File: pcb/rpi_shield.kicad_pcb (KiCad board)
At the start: 2 copper layers, 65 x 56 mm, 61 parts, among them P101 CONN_01X08, P102 CONN_02X20, P301 USB_OTG, Q201 Q_NMOS_GDSD, Q202 Q_NMOS_GDSD, Q203 Q_NMOS_GDSD, Q204 Q_NMOS_GDSD, Q205 NPN, Q206 NPN, Q207 NPN, Q208 NPN, Q301 FT230XS-R, U201 LM2902N, U202 MAX5813

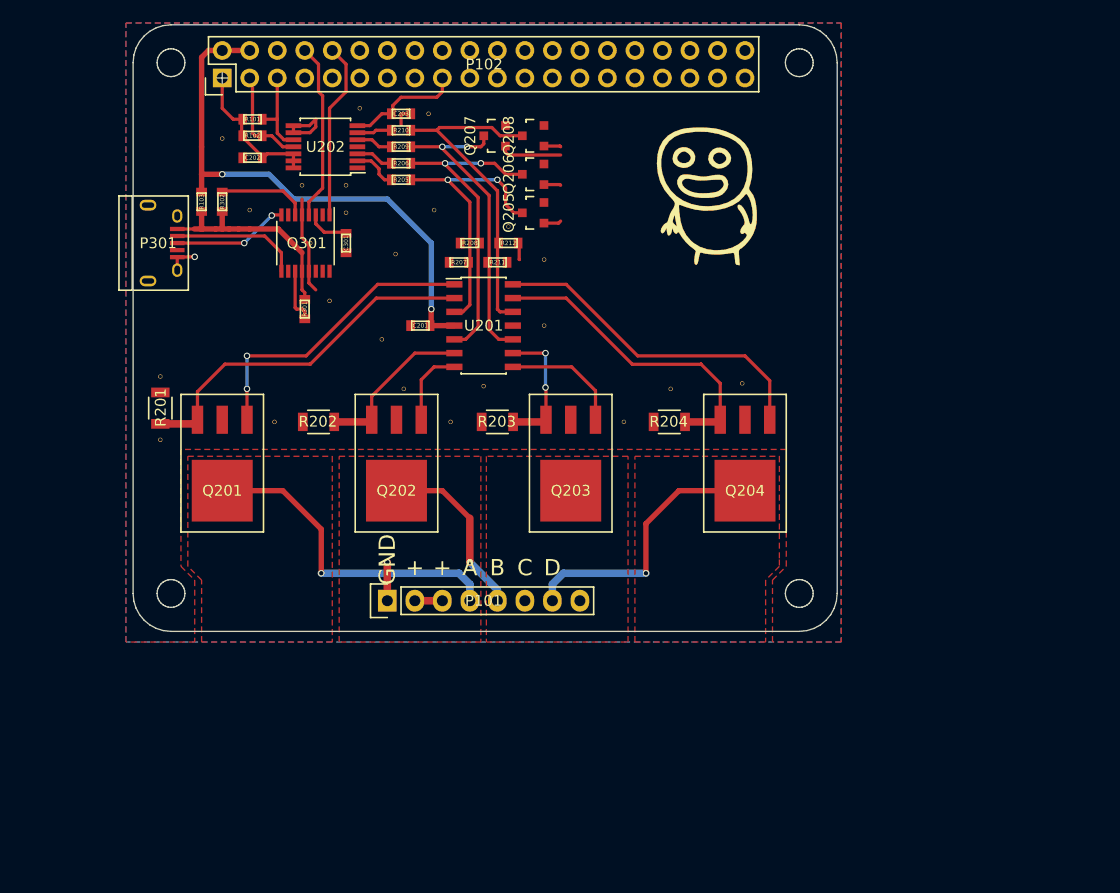
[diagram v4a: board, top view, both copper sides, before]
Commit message: removed resistor dividors, added cap to usb
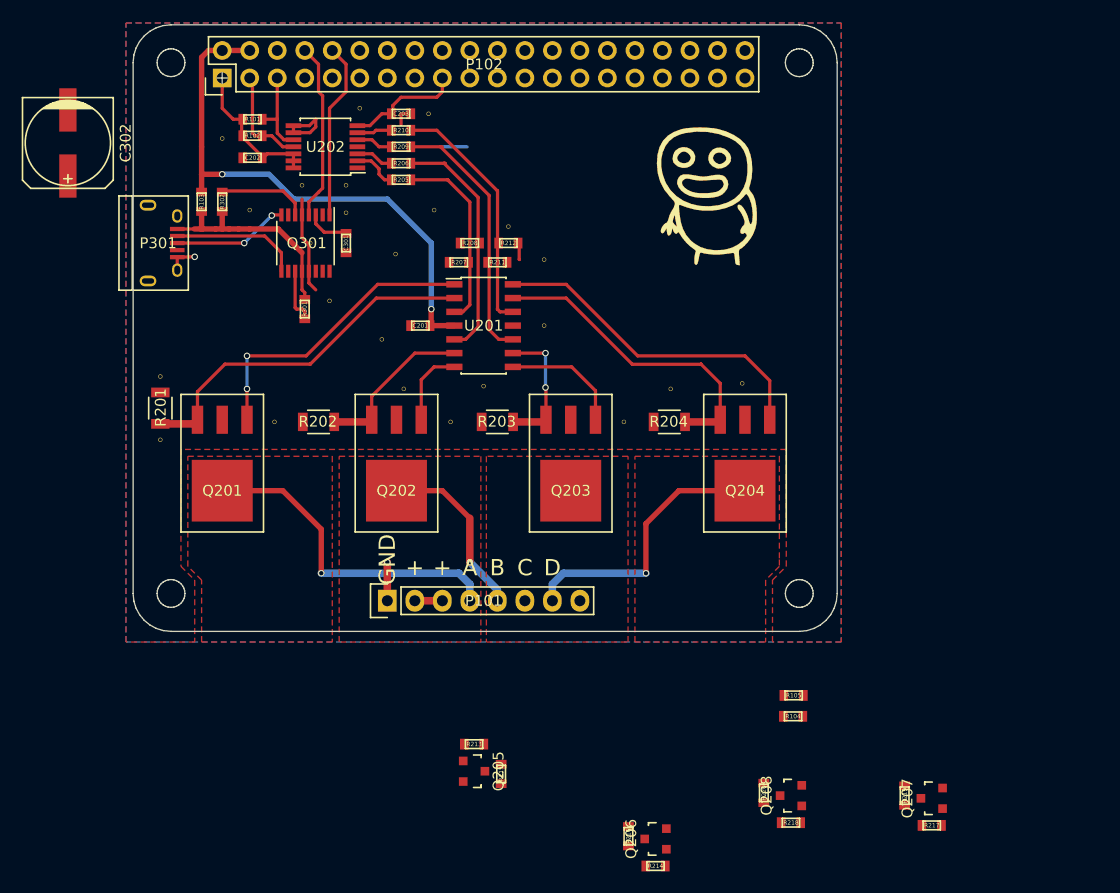
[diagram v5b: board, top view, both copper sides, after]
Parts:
- added C302: CP, Capacitors_SMD:c_elec_8x5.4, F.Cu at (115.8, 86.0)
- added R104: R, netl:SMD_0603, F.Cu at (182.7, 138.9)
- added R105: R, netl:SMD_0603, F.Cu at (182.8, 137.0)
- added R213: R, netl:SMD_0603, F.Cu at (153.2, 141.5)
- added R214: R, netl:SMD_0603, F.Cu at (170.0, 152.8)
- added R215: R, netl:SMD_0603, F.Cu at (155.8, 144.2)
- added R216: R, netl:SMD_0603, F.Cu at (167.5, 150.0)
- added R217: R, netl:SMD_0603, F.Cu at (195.5, 149.0)
- added R218: R, netl:SMD_0603, F.Cu at (182.5, 148.8)
- added R219: R, netl:SMD_0603, F.Cu at (193.0, 146.2)
- added R220: R, netl:SMD_0603, F.Cu at (180.0, 146.0)
- moved Q207 73.3 mm to (195.5, 146.5)
- moved Q208 65.4 mm to (182.5, 146.2)
- moved Q206 62.4 mm to (170.0, 150.2)
- moved Q205 51.8 mm to (153.2, 144.0), turned to 270 degrees
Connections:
- net MISO renamed /MISO
- net MOSI renamed /MOSI
- net RESET renamed /RESET
- net SCK renamed /SCK
- P102 pad 3: /LED driver/SDA -> /SDA
- P102 pad 5: /LED driver/SCL -> /SCL
- Q205 pad 3: Net-(Q205-Pad3) -> Net-(Q201-Pad1)
- Q206 pad 3: Net-(Q206-Pad3) -> Net-(Q202-Pad1)
- Q207 pad 3: Net-(Q207-Pad3) -> Net-(Q203-Pad1)
- Q208 pad 3: Net-(Q208-Pad3) -> Net-(Q204-Pad1)
- R101 pad 2: /LED driver/SCL -> /SDA
- R102 pad 2: /LED driver/SDA -> /SCL
- R205 pad 1: Net-(Q205-Pad3) -> Net-(R205-Pad1)
- R206 pad 1: Net-(Q206-Pad3) -> Net-(R206-Pad1)
- R207 pad 1: Net-(Q205-Pad3) -> Net-(R205-Pad1)
- R208 pad 1: Net-(Q206-Pad3) -> Net-(R206-Pad1)
- R209 pad 1: Net-(Q207-Pad3) -> Net-(R209-Pad1)
- R210 pad 1: Net-(Q208-Pad3) -> Net-(R210-Pad1)
- R211 pad 1: Net-(Q207-Pad3) -> Net-(R209-Pad1)
- R212 pad 1: Net-(Q208-Pad3) -> Net-(R210-Pad1)
- U201 pad 1: Net-(Q201-Pad1) -> Net-(R215-Pad2)
- U201 pad 10: Net-(Q207-Pad3) -> /LED driver/C
- U201 pad 12: Net-(Q208-Pad3) -> /LED driver/D
- U201 pad 14: Net-(Q204-Pad1) -> Net-(R220-Pad2)
- U201 pad 3: Net-(Q205-Pad3) -> /LED driver/A
- U201 pad 5: Net-(Q206-Pad3) -> /LED driver/B
- U201 pad 7: Net-(Q202-Pad1) -> Net-(R216-Pad2)
- U201 pad 8: Net-(Q203-Pad1) -> Net-(R219-Pad2)
- U202 pad 10: /LED driver/SCL -> /SCL
- U202 pad 11: /LED driver/SDA -> /SDA
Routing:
- net Net-(Q208-Pad3): track 31.0 -> 0.00 mm
- net Net-(Q206-Pad3): track 30.4 -> 0.00 mm, vias 2 -> 0
- net Net-(Q207-Pad3): track 29.2 -> 0.00 mm, vias 2 -> 0
- net Net-(Q205-Pad3): track 26.5 -> 0.00 mm, vias 2 -> 0
- net Net-(R209-Pad1): track 0.00 -> 21.9 mm
- net Net-(R210-Pad1): track 0.00 -> 21.1 mm
- net Net-(R206-Pad1): track 0.00 -> 20.1 mm
- net Net-(R215-Pad2): track 0.00 -> 16.4 mm
- net Net-(Q201-Pad1): track 28.1 -> 11.7 mm
- net Net-(R205-Pad1): track 0.00 -> 15.8 mm
- net /SDA: track 0.00 -> 11.4 mm
- net /LED driver/SDA: track 9.49 -> 0.00 mm
- net /LED driver/SCL: track 8.12 -> 0.00 mm
- net /SCL: track 0.00 -> 6.21 mm
- net Net-(Q207-Pad1): track 5.77 -> 0.00 mm
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
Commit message: added mcu
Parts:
- removed R205, R206, R207, R208, R209, R210, R211, R212: 10k, netl:SMD_0603
- removed the VIA at (178.0, 108.2)
- removed the VIA at (124.3, 113.4)
- removed the VIA at (156.4, 93.7)
- removed the VIA at (149.6, 92.2)
- removed the VIA at (130.0, 85.6)
- removed the VIA at (154.1, 108.4)
- removed the VIA at (159.7, 96.8)
- removed the VIA at (149.1, 83.3)
- removed the VIA at (159.7, 102.9)
- removed the VIA at (146.0, 96.3)
- removed the VIA at (142.7, 82.8)
- removed the VIA at (141.4, 89.9)
- removed the VIA at (137.4, 89.9)
- removed the VIA at (141.4, 92.4)
- removed the VIA at (171.4, 108.7)
- removed the VIA at (146.8, 108.7)
- removed the VIA at (144.7, 104.1)
- removed the VIA at (139.9, 100.6)
- removed the VIA at (132.5, 92.2)
- added C401: C, netl:SMD_0603, F.Cu at (155.4, 100.0)
- added IC401: ATMEGA48-M, Housings_QFP:TQFP-32_7x7mm_Pitch0.8mm, F.Cu at (155.0, 92.5)
- added P401: CONN_01X01, netl:1Pin_small, F.Cu at (155.0, 86.0)
- added P402: CONN_01X01, netl:1Pin_small, F.Cu at (157.0, 86.0)
- added P403: CONN_01X01, netl:1Pin_small, F.Cu at (153.0, 86.0)
- added P404: CONN_01X01, netl:1Pin_small, F.Cu at (163.0, 91.0)
- added P405: CONN_01X01, netl:1Pin_small, F.Cu at (163.0, 89.0)
- added P406: CONN_01X01, netl:1Pin_small, F.Cu at (163.0, 87.0)
- added P407: CONN_01X01, netl:1Pin_small, F.Cu at (158.0, 100.0)
- added P408: CONN_01X01, netl:1Pin_small, F.Cu at (160.0, 100.0)
- added P409: CONN_01X01, netl:1Pin_small, F.Cu at (149.0, 100.0)
- added P410: CONN_01X01, netl:1Pin_small, F.Cu at (151.0, 100.0)
- added P411: CONN_01X01, netl:1Pin_small, F.Cu at (153.0, 100.0)
- added P412: CONN_01X01, netl:1Pin_small, F.Cu at (163.0, 97.0)
- added P413: CONN_01X01, netl:1Pin_small, F.Cu at (163.0, 95.0)
- added P414: CONN_01X01, netl:1Pin_small, F.Cu at (163.0, 93.0)
- added VIA: via, netl:via, F.Cu at (124.7, 122.8)
- added VIA: via, netl:via, F.Cu at (157.7, 102.4)
- added VIA: via, netl:via, F.Cu at (149.9, 102.4)
- added VIA: via, netl:via, F.Cu at (140.9, 103.2)
- added VIA: via, netl:via, F.Cu at (144.9, 108.2)
- added VIA: via, netl:via, F.Cu at (128.9, 108.2)
- added VIA: via, netl:via, F.Cu at (177.1, 108.6)
- added VIA: via, netl:via, F.Cu at (181.1, 105.4)
- added VIA: via, netl:via, F.Cu at (160.9, 107.6)
- added VIA: via, netl:via, F.Cu at (174.9, 102.0)
- added VIA: via, netl:via, F.Cu at (176.8, 89.6)
- added VIA: via, netl:via, F.Cu at (137.5, 115.8)
- added VIA: via, netl:via, F.Cu at (174.2, 90.4)
- added VIA: via, netl:via, F.Cu at (171.9, 94.6)
- added VIA: via, netl:via, F.Cu at (177.8, 94.6)
- added VIA: via, netl:via, F.Cu at (182.5, 102.2)
- added VIA: via, netl:via, F.Cu at (167.1, 101.2)
- added VIA: via, netl:via, F.Cu at (179.3, 102.0)
- added VIA: via, netl:via, F.Cu at (173.3, 108.8)
- added VIA: via, netl:via, F.Cu at (140.9, 108.2)
- added VIA: via, netl:via, F.Cu at (132.9, 101.6)
- added VIA: via, netl:via, F.Cu at (146.3, 97.0)
- added VIA: via, netl:via, F.Cu at (152.7, 116.0)
- added VIA: via, netl:via, F.Cu at (150.5, 97.0)
- added VIA: via, netl:via, F.Cu at (159.3, 97.0)
- added VIA: via, netl:via, F.Cu at (154.5, 92.4)
- added VIA: via, netl:via, F.Cu at (151.7, 85.0)
- added VIA: via, netl:via, F.Cu at (164.3, 85.2)
- added VIA: via, netl:via, F.Cu at (171.9, 85.2)
- added VIA: via, netl:via, F.Cu at (171.9, 82.2)
- added VIA: via, netl:via, F.Cu at (164.3, 82.2)
- added VIA: via, netl:via, F.Cu at (151.7, 82.2)
- added VIA: via, netl:via, F.Cu at (143.5, 82.2)
- added VIA: via, netl:via, F.Cu at (169.5, 115.8)
- added VIA: via, netl:via, F.Cu at (137.7, 82.2)
- added VIA: via, netl:via, F.Cu at (139.5, 85.6)
- added VIA: via, netl:via, F.Cu at (129.7, 83.6)
- added VIA: via, netl:via, F.Cu at (136.9, 89.2)
- added VIA: via, netl:via, F.Cu at (143.7, 91.6)
- added VIA: via, netl:via, F.Cu at (142.9, 94.2)
- added VIA: via, netl:via, F.Cu at (134.1, 97.2)
- added VIA: via, netl:via, F.Cu at (128.7, 97.8)
- added VIA: via, netl:via, F.Cu at (131.3, 95.8)
- added VIA: via, netl:via, F.Cu at (133.9, 93.4)
- added VIA: via, netl:via, F.Cu at (183.5, 121.6)
- added VIA: via, netl:via, F.Cu at (177.1, 84.8)
- added VIA: via, netl:via, F.Cu at (167.5, 94.6)
- added VIA: via, netl:via, F.Cu at (162.7, 99.4)
- added VIA: via, netl:via, F.Cu at (157.7, 107.6)
- moved R104 57.1 mm to (146.2, 95.0)
- moved R105 57.0 mm to (146.2, 93.2)
- moved R217 53.2 mm to (163.2, 106.8), turned to 0 degrees
- moved R214 51.3 mm to (147.2, 106.8), turned to 0 degrees
- moved Q207 49.3 mm to (163.2, 109.2), turned to 270 degrees
- moved Q206 46.9 mm to (147.2, 109.2), turned to 270 degrees
- moved R219 46.8 mm to (165.8, 108.2)
- moved R216 45.4 mm to (149.8, 108.2)
- moved R215 42.2 mm to (133.8, 108.2), turned to 90 degrees
- moved R218 41.9 mm to (179.5, 107.0), turned to 0 degrees
- moved Q205 41.1 mm to (131.2, 109.2)
- moved R213 41.1 mm to (131.2, 106.8)
- moved C202 38.6 mm to (171.4, 88.0), turned to 90 degrees
- moved R220 37.6 mm to (182.0, 108.5)
- moved Q208 36.9 mm to (179.5, 109.5), turned to 270 degrees
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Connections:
- net /SCL renamed /LED driver/SCL
- net /SDA renamed /LED driver/SDA
- P102 pad 15: /RESET -> /MicroController/~RESET
- P102 pad 19: /MOSI -> /MicroController/MOSI
- P102 pad 21: /MISO -> /MicroController/MISO
- P102 pad 23: /SCK -> /MicroController/SCK
- R104 pad 2: Net-(R104-Pad2) -> /MicroController/TX
- R105 pad 2: Net-(R105-Pad2) -> /MicroController/RX
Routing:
- net /LED driver/SCL: track 6.21 -> 60.5 mm, vias 0 -> 2
- net /LED driver/SDA: track 11.4 -> 59.7 mm
- net /LED driver/PWMD: track 0.00 -> 46.8 mm, vias 0 -> 2
- net /LED driver/PWMA: track 0.00 -> 39.8 mm, vias 0 -> 2
- net 3v3: track 24.3 -> 59.9 mm, vias 0 -> 2
- net /LED driver/PWMC: track 0.00 -> 33.1 mm, vias 0 -> 2
- net Net-(R215-Pad2): track 16.4 -> 44.0 mm, vias 0 -> 2
- net Net-(Q202-Pad3): track 15.1 -> 40.7 mm
- net Net-(Q201-Pad3): track 33.7 -> 58.4 mm
- net /LED driver/PWMB: track 0.00 -> 23.2 mm, vias 0 -> 2
- net Net-(R216-Pad2): track 1.87 -> 24.0 mm
- net Net-(R209-Pad1): track 21.9 -> 0.00 mm
- net Net-(R210-Pad1): track 21.1 -> 0.00 mm
- net Net-(Q204-Pad1): track 26.6 -> 5.95 mm
- net Net-(R206-Pad1): track 20.1 -> 0.00 mm
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
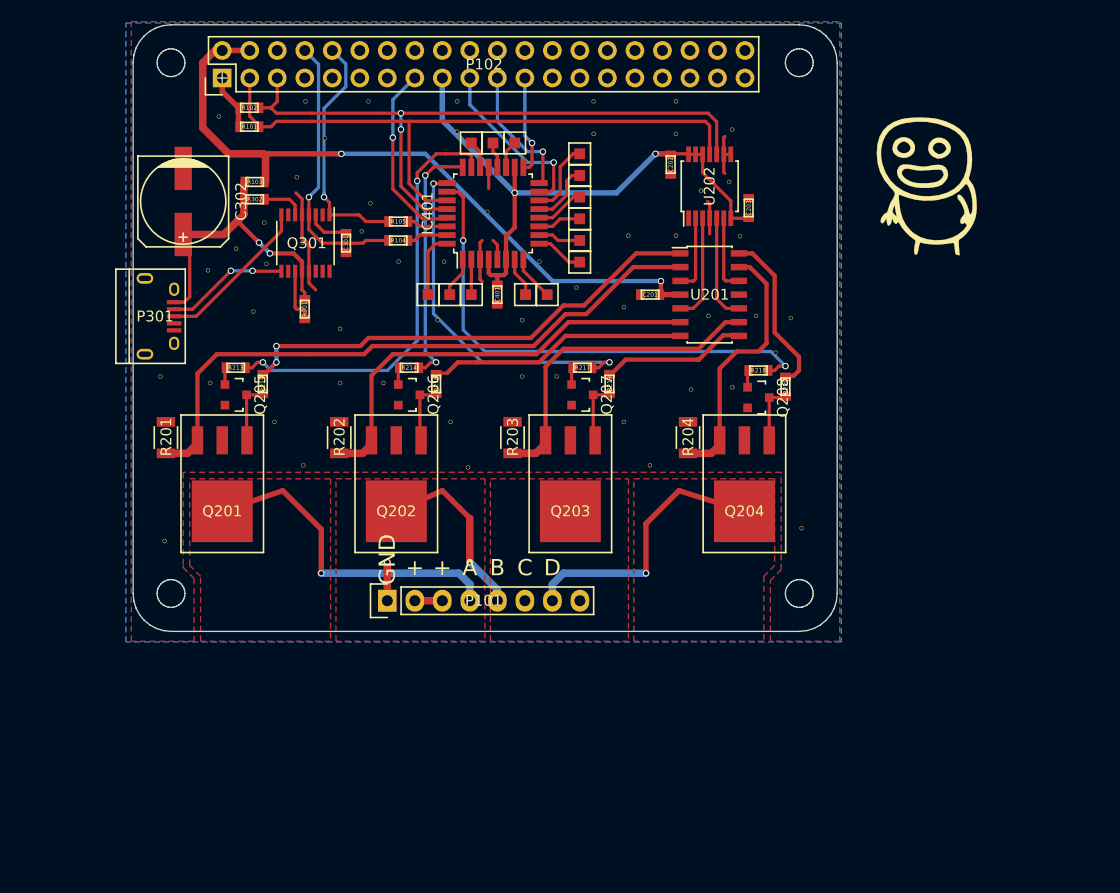
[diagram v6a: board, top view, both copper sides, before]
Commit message: added the voltage dividers back to the constant-current control
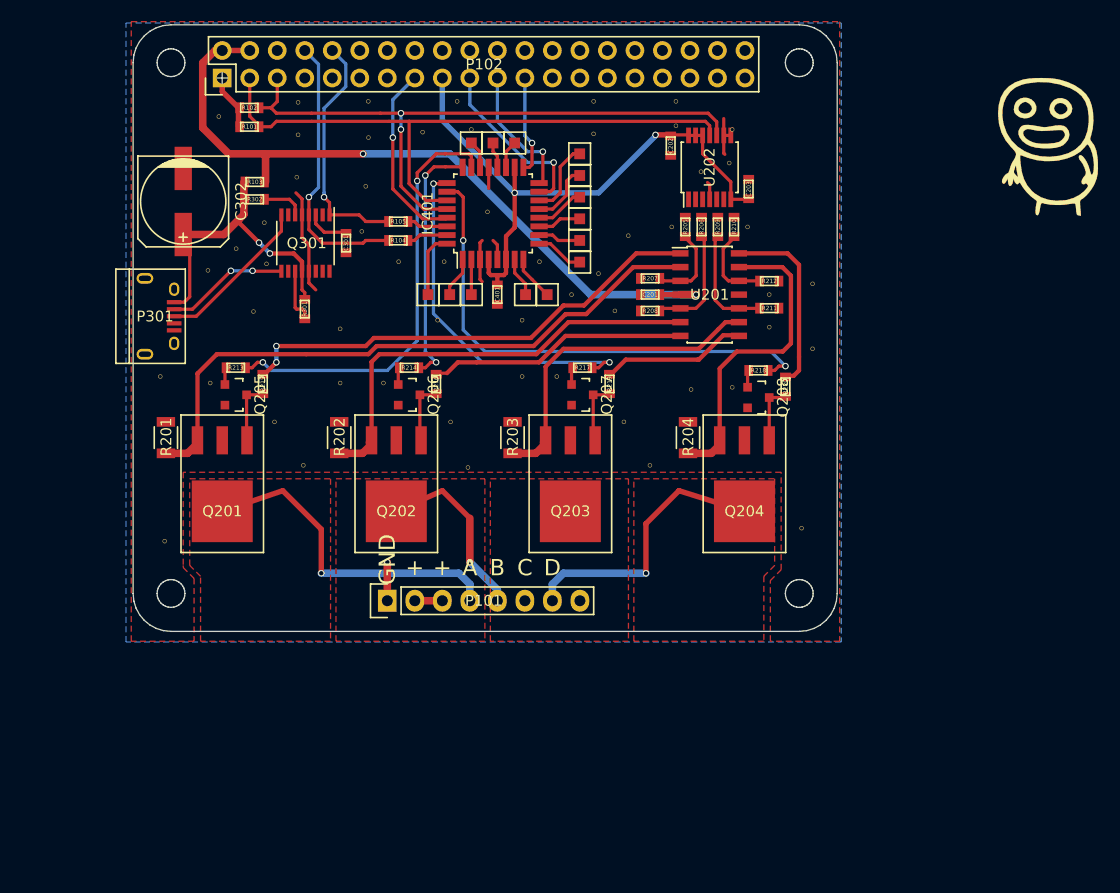
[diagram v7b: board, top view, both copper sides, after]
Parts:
- removed the VIA at (174.9, 102.0)
- removed the VIA at (137.4, 95.2)
- added R205: R, netl:SMD_0603, F.Cu at (172.8, 93.8)
- added R206: R, netl:SMD_0603, F.Cu at (174.2, 93.8)
- added R207: R, netl:SMD_0603, F.Cu at (169.5, 98.5)
- added R208: R, netl:SMD_0603, F.Cu at (169.5, 101.5)
- added R209: R, netl:SMD_0603, F.Cu at (175.8, 93.8)
- added R210: R, netl:SMD_0603, F.Cu at (177.2, 93.8)
- added R211: R, netl:SMD_0603, F.Cu at (180.5, 101.2)
- added R212: R, netl:SMD_0603, F.Cu at (180.5, 98.8)
- added VIA: via, netl:via, F.Cu at (164.7, 98.1)
- added VIA: via, netl:via, F.Cu at (137.0, 85.2)
- added VIA: via, netl:via, F.Cu at (148.5, 85.0)
- added VIA: via, netl:via, F.Cu at (180.5, 103.0)
- VIA: moved to B.Cu
- moved G*** 11.8 mm to (206.2, 86.3) (x2)
- moved VIA 6.00 mm to (184.5, 99.0)
- moved VIA 4.02 mm to (143.5, 85.5)
- moved VIA 3.43 mm to (184.5, 105.0)
- moved VIA 2.93 mm to (180.5, 100.0)
- moved C202 1.75 mm to (171.4, 86.2)
- moved C203 1.75 mm to (178.6, 90.2)
- moved U202 1.75 mm to (175.0, 88.2)
- moved VIA 1.75 mm to (176.8, 87.8)
- moved VIA 1.75 mm to (174.2, 88.7)
- moved VIA 1.62 mm to (143.2, 90.0)
- moved VIA 1.33 mm to (153.0, 84.8)
- moved VIA 1.10 mm to (178.5, 93.8)
- moved VIA 0.90 mm to (166.2, 101.5)
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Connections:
- U201 pad 10: /LED driver/C -> Net-(R209-Pad2)
- U201 pad 12: /LED driver/D -> Net-(R210-Pad2)
- U201 pad 3: /LED driver/A -> Net-(R205-Pad2)
- U201 pad 5: /LED driver/B -> Net-(R206-Pad2)
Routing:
- net Net-(R209-Pad2): track 0.00 -> 10.3 mm
- net Net-(R206-Pad2): track 0.00 -> 10.3 mm
- net /LED driver/C: track 9.86 -> 0.00 mm
- net /LED driver/B: track 9.86 -> 0.00 mm
- net Net-(R205-Pad2): track 0.00 -> 7.49 mm
- net Net-(R210-Pad2): track 0.00 -> 7.37 mm
- net /LED driver/A: track 7.09 -> 0.00 mm
- net /LED driver/D: track 7.07 -> 0.00 mm
- net Net-(Q204-Pad3): track 24.9 -> 29.9 mm
- net 5V: track 64.6 -> 68.7 mm
- net Net-(R220-Pad2): track 15.3 -> 17.2 mm
- net /LED driver/SDA: track 59.7 -> 57.9 mm
- net /LED driver/SCL: track 60.5 -> 58.8 mm
- net GND: track 28.3 -> 26.7 mm
- net 3v3: track 59.9 -> 60.7 mm
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
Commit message: added the damn resistors... again.
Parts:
- removed the VIA at (149.9, 102.4)
- removed the VIA at (150.5, 97.0)
- removed the VIA at (159.3, 97.0)
- removed the VIA at (142.9, 94.2)
- removed the VIA at (134.1, 97.2)
- removed the VIA at (128.7, 97.8)
- removed the VIA at (131.3, 95.8)
- moved P101 14.1 mm to (144.3, 142.3)
- moved U202 0.15 mm to (175.0, 88.1)
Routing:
- net /LED driver/DrainA: track 30.7 -> 0.00 mm, vias 1 -> 0
- net /LED driver/DrainD: track 27.3 -> 1.52 mm, vias 1 -> 0
- net /LED driver/DrainB: track 16.9 -> 0.00 mm, vias 1 -> 0
- net GND: track 26.7 -> 23.2 mm, vias 1 -> 0
- net VCC: track 2.54 -> 0.00 mm
- net /LED driver/A: track 0.00 -> 2.31 mm
- net /LED driver/D: track 0.00 -> 2.21 mm
- net /LED driver/C: track 0.00 -> 1.74 mm
- net /LED driver/B: track 0.00 -> 1.74 mm
